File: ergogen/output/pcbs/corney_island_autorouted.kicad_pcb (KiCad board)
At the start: 2 copper layers, 133.8 x 91.7 mm, 101 parts

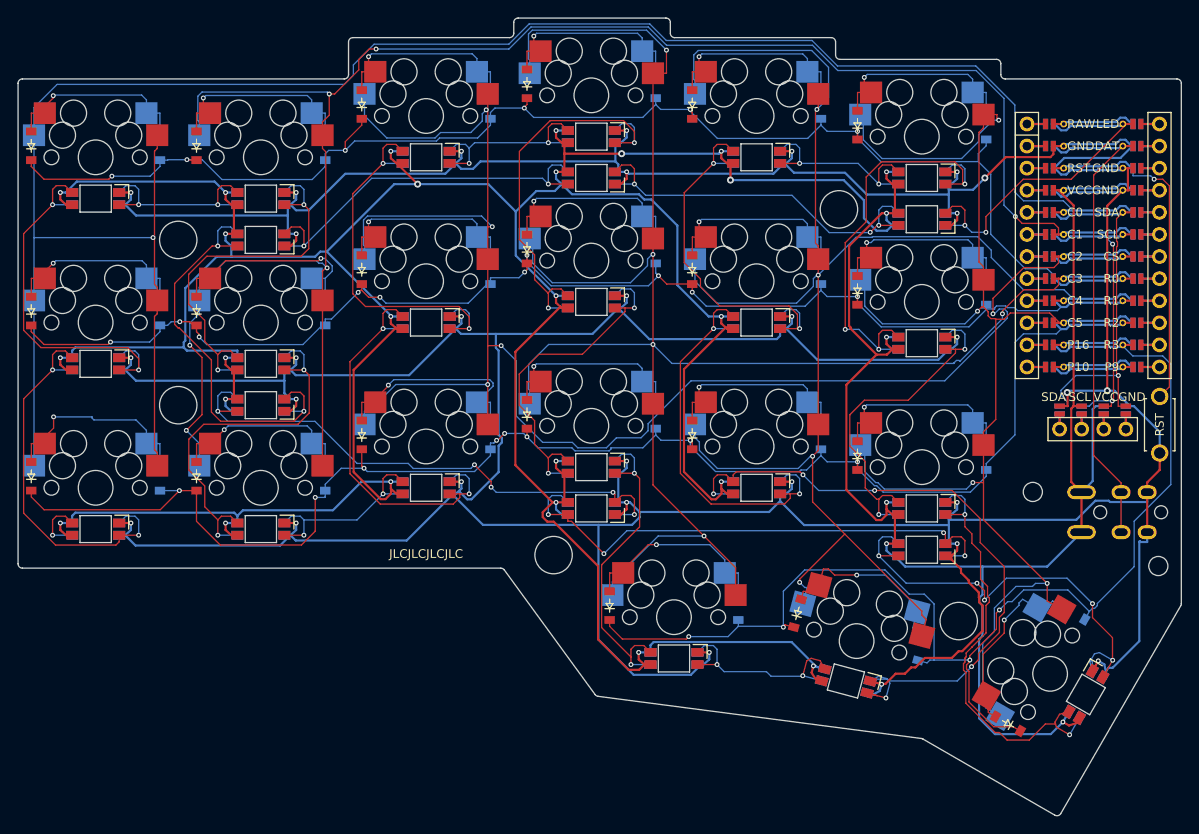
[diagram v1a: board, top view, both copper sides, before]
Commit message: Switch to KiCad 8 PCB template and require Ergogen v4.1.0
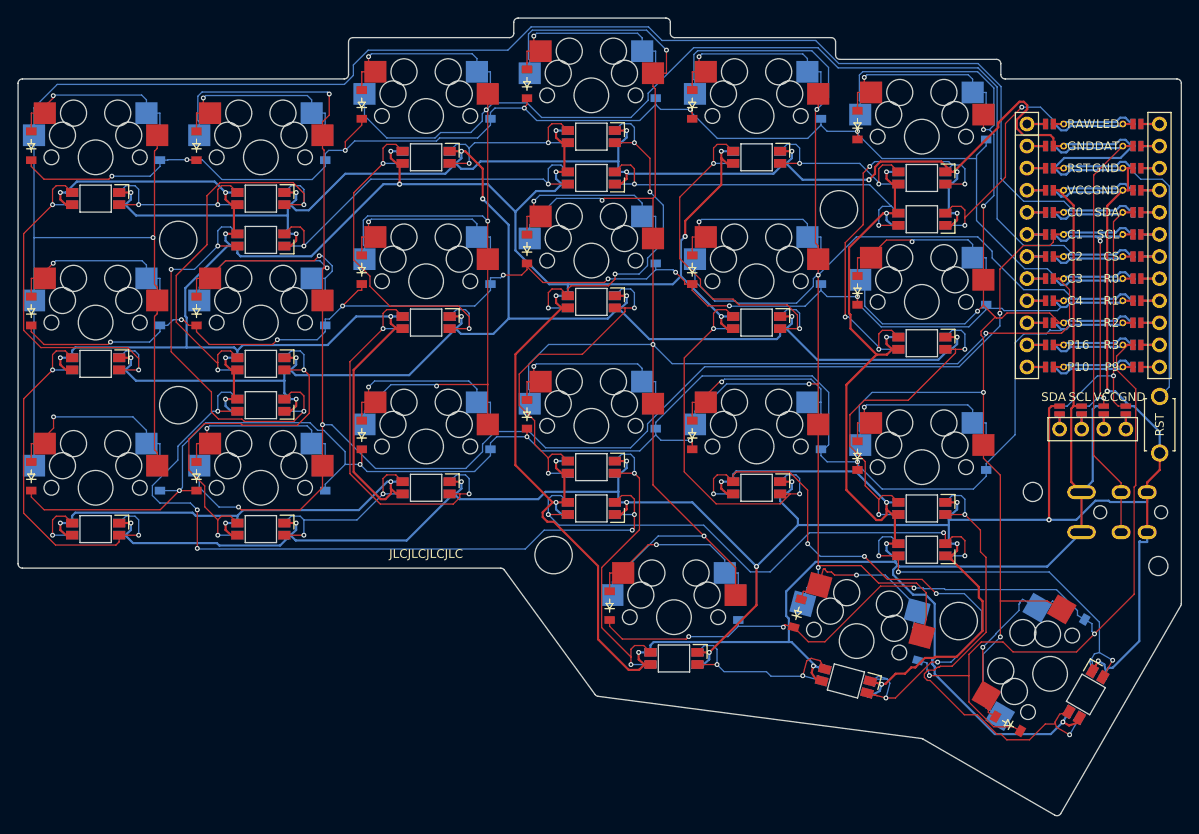
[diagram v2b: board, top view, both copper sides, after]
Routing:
- net ULED_4: track 64.8 -> 89.8 mm
- net R2: track 175.5 -> 191.0 mm, vias 8 -> 5
- net LED_11: track 47.7 -> 41.2 mm, vias 2 -> 4
- net VCC: track 644.6 -> 638.3 mm, vias 30 -> 29
- net ULED_6: track 52.0 -> 45.7 mm, vias 5 -> 3
- net LED_1: track 51.2 -> 57.0 mm
- net LED_17: track 44.5 -> 49.8 mm
- net R3: track 142.5 -> 147.9 mm, vias 4 -> 5
- net LED_7: track 78.4 -> 73.2 mm, vias 5 -> 6
- net LED: track 41.8 -> 36.8 mm
- net ULED_5: track 61.6 -> 64.9 mm, vias 4 -> 3
- net LED_3: track 50.7 -> 47.5 mm, vias 3 -> 4
- net SDA: track 43.9 -> 41.4 mm
- net C3: track 205.9 -> 207.8 mm
- net SCL: track 34.6 -> 32.8 mm
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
